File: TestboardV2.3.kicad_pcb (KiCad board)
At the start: 2 copper layers, 61 x 100 mm, 149 parts, among them IC1 BME680, IC2 MAX17048G+, IC3 LTC2954CTS8-1#TRMPBF, IC4 CN3791, IC5 FS312F-G, J10 Conn_01x04, J11 Conn_01x02, J12 Conn_01x02, J13 USB_C_Receptacle_USB2.0 USB41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, J2 Conn_01x04_MountingPin, J3 Conn_01x04_MountingPin, J4 Conn_01x04_MountingPin, J5 Conn_01x04_MountingPin, J6 Conn_01x04_MountingPin, J7 Conn_01x04, J8 Conn_01x02, J9 Conn_01x03, Q1 UMH3N, Q2 DMG2301L, Q3 AO3401A, Q4 FS8205, Q5 AO3400, SW1 SW_Push, SW2 SW_Push, SW4 SW_Push, U1 ESP32-WROOM-32D, U10 PC817, U11 PC817, U12 CP2102N-A02-GQFN24, U13 XC6220B331MR, U15 MCP73831-2-OT, U2 PC817, U3 PC817, U4 PC817, U5 PC817, U6 PC817, U7 PC817, U8 PC817, U9 PC817

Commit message: Testboard V2.3
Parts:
- removed the C12 at (152.8, 82.4)
- removed the C13 at (152.8, 81.0)
- removed the IC1 at (154.0, 78.5)
- removed Q5: AO3400, Empreintes:SOT95P280X125-3N
- removed R32: 1.2K, Resistor_SMD:R_0603_1608Metric
- removed SW4: SW_Push, Empreintes:PTS636SL43SMTRLFS
- added C20: 0.1µF, Capacitor_SMD:C_0603_1608Metric, F.Cu at (153.8, 79.4)
- added C24: 10µF, Capacitor_SMD:C_0805_2012Metric, F.Cu at (113.8, 117.2)
- added C25: 10µF, Capacitor_SMD:C_0805_2012Metric, F.Cu at (122.3, 119.2)
- added IC6: SHT41-AD1B-R3, Empreintes:SHT41AD1BR3, F.Cu at (155.5, 78.1)
- C10, C8: value TBD -> 0.150µF
- R23: value 140K -> 30K
- R25: value 2K -> 10K
- R28: value 0.05R -> 0.24R
- moved J8 2.20 mm to (155.2, 146.8), turned to 270 degrees
- moved J12 2.18 mm to (155.3, 140.2), turned to 270 degrees
- moved REF** 1.50 mm to (108.9, 92.6)
- moved C9 1.21 mm to (115.4, 117.4)
- moved REF** 1.19 mm to (102.3, 92.3)
- moved C11 0.87 mm to (120.7, 119.0)
- moved U13 0.87 mm to (118.0, 119.1)
- moved G*** 0.53 mm to (130.6, 150.9)
- moved G*** 0.27 mm to (137.1, 143.1)
- moved Q3 0.09 mm to (124.6, 157.3), turned to 270 degrees
- renumbered C19 to C12, C14 to C13, C21 to C14, C22 to C19, C23 to C21, C25 to C22, C26 to C23, D9 to D10, D10 to D11, D11 to D12, D12 to D13, D13 to D8, D8 to D9, IC4 to IC1, IC5 to IC4, J11 to J1
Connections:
- C27 pad 2: Net-(C27-Pad2) -> VBAT-
- D13 pad 2: Net-(D12-Pad2) -> Net-(D13-Pad2)
- IC4 pad 6: Net-(C27-Pad2) -> VBAT-
- J12 pad 1: VBAT -> GND
- J12 pad 2: GND -> VBAT
- J8 pad 1: VBAT -> VBAT-
- J8 pad 2: VBAT- -> VBAT
- Q3 pad 2: Net-(D12-Pad2) -> Vsolar
- Q3 pad 3: Vsolar -> Net-(D13-Pad2)
- Q4 pad 1: Net-(C27-Pad2) -> VBAT-
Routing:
- net Net-(C27-Pad2): track 28.0 -> 0.00 mm
- net Net-(D12-Pad2): track 23.2 -> 0.00 mm
- net VBAT-: track 7.49 -> 30.4 mm
- net Net-(D13-Pad2): track 0.00 -> 22.0 mm
- net GND: track 30.6 -> 41.7 mm, vias 204 -> 200
- net Net-(Q5-Pad1): track 3.18 -> 0.00 mm
- net Net-(IC1-Pad10): track 5.69 -> 2.60 mm
- net SDA: track 120.3 -> 123.1 mm
- net +3V3: track 229.0 -> 226.4 mm
- net Vsolar: track 50.9 -> 48.9 mm
- net VBAT: track 111.9 -> 113.1 mm
- net CE: track 24.7 -> 25.7 mm
- net +5V: track 154.4 -> 155.2 mm
- net SCL: track 129.6 -> 129.1 mm
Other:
- outline, holes or cut-outs redrawn
- board text added: "Test board V2.2 with: ESP32-WROOM-32E CP2102N XC6220B33 PC817 SHT41 LTC2954CTS8 MCP73831 MAX17048G+ CN3791 USB-C"
- board text removed: "BME680"
- board text removed: "Test board V2.2 with: ESP32-WROOM-32E CP2102N XC6220B33 PC817 BME680 LTC2954CTS8 MCP73831 MAX17048G+ CN3791 USB-C"

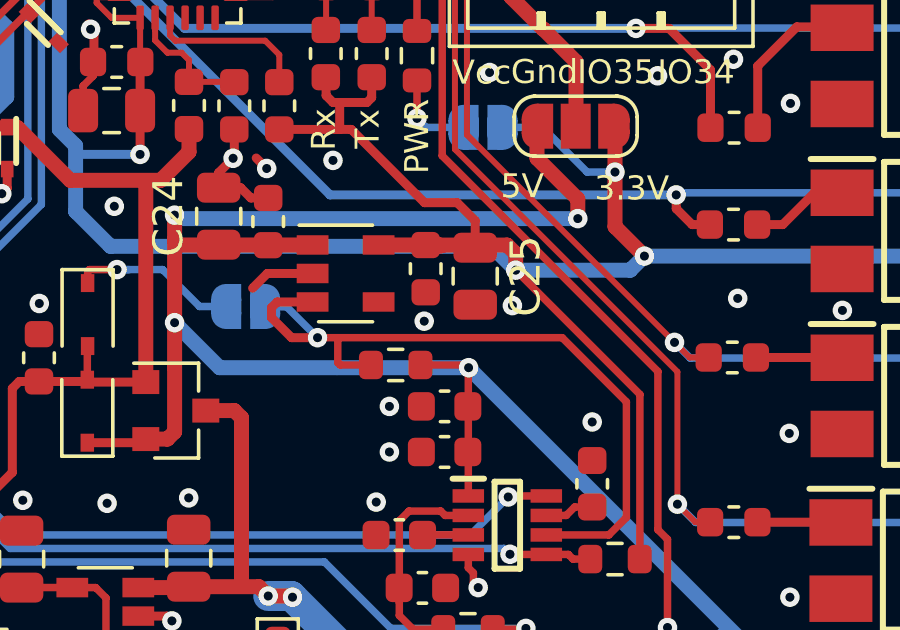
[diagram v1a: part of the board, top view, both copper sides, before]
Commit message: Gnd pad correction
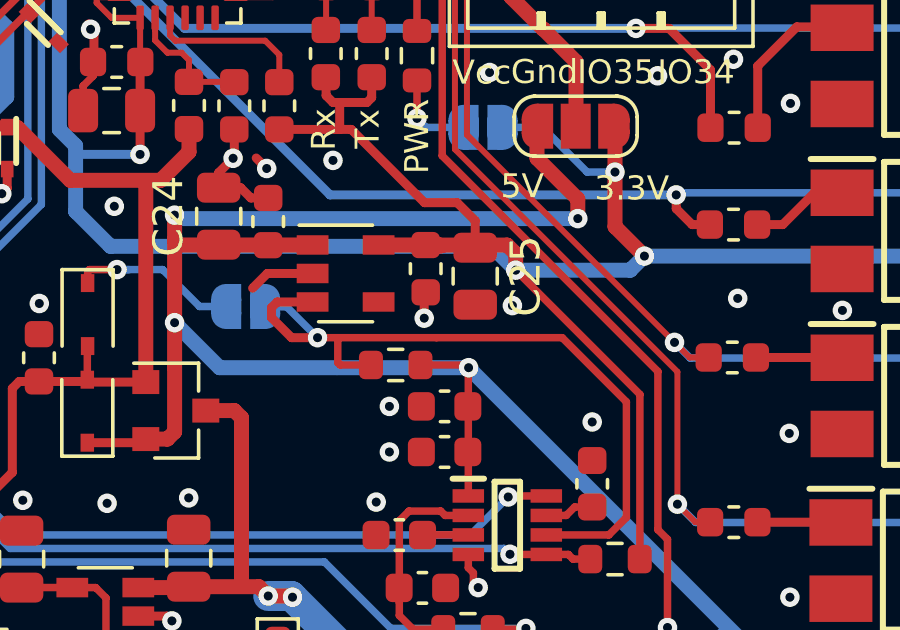
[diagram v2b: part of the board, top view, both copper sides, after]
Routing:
- net GND: track 41.7 -> 42.5 mm
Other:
- rule trace_min: 0.2 -> 0

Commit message: serigraphy correction
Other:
- board text added: "Test board V2.3 with: ESP32-WROOM-32E CP2102N XC6220B33 PC817 SHT41 LTC2954CTS8 MCP73831 MAX17048G+ CN3791 USB-C"
- board text removed: "Test board V2.2 with: ESP32-WROOM-32E CP2102N XC6220B33 PC817 SHT41 LTC2954CTS8 MCP73831 MAX17048G+ CN3791 USB-C"
